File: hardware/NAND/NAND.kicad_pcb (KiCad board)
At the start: 2 copper layers, 53.3 x 86.4 mm, 10 parts, among them J1 Conn_02x33_Odd_Even, J2 Conn_02x33_Odd_Even, J3 DBG, J4 Left, J5 Right

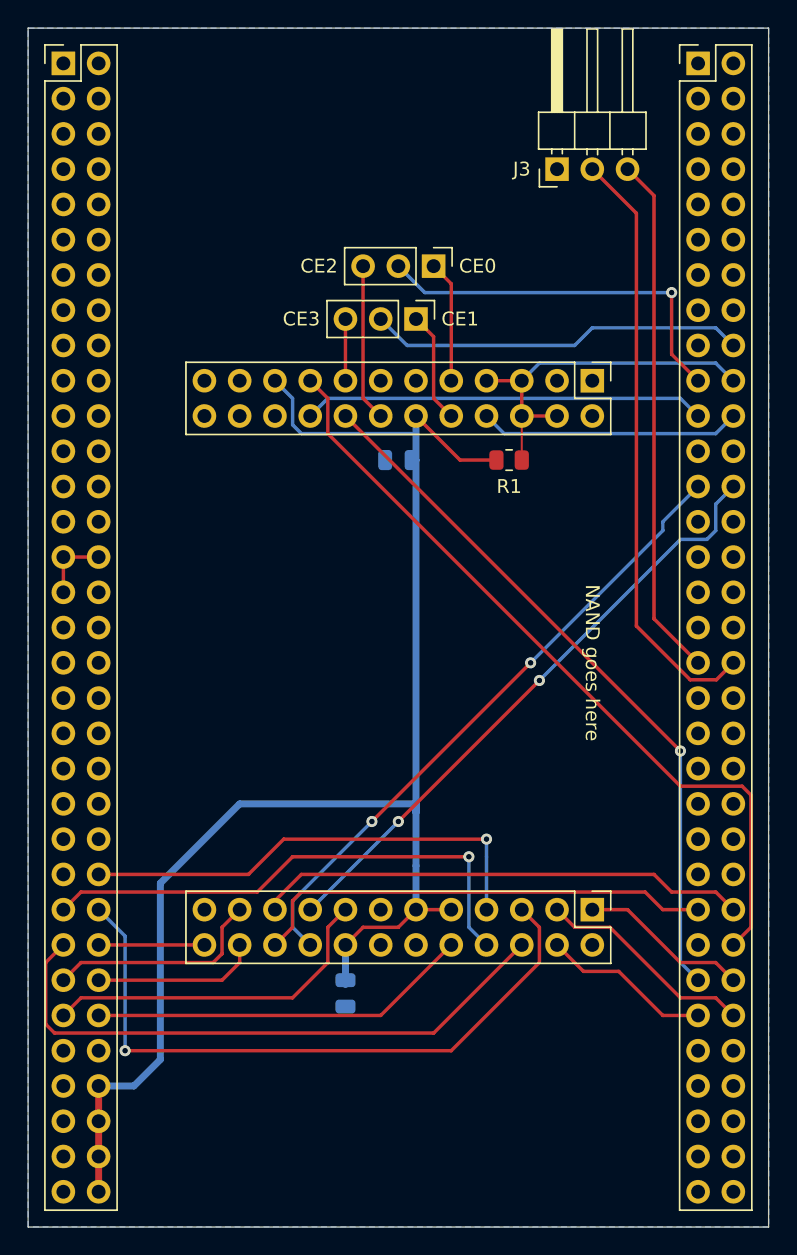
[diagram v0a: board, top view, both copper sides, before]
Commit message: hardware: NAND top to rev.B
+ Modified J3 DBG to break out SWO and GPIO pins

+ FSMC CE2 can be switched to any of NAND CEx

+ Added pull-ups for NAND CEx
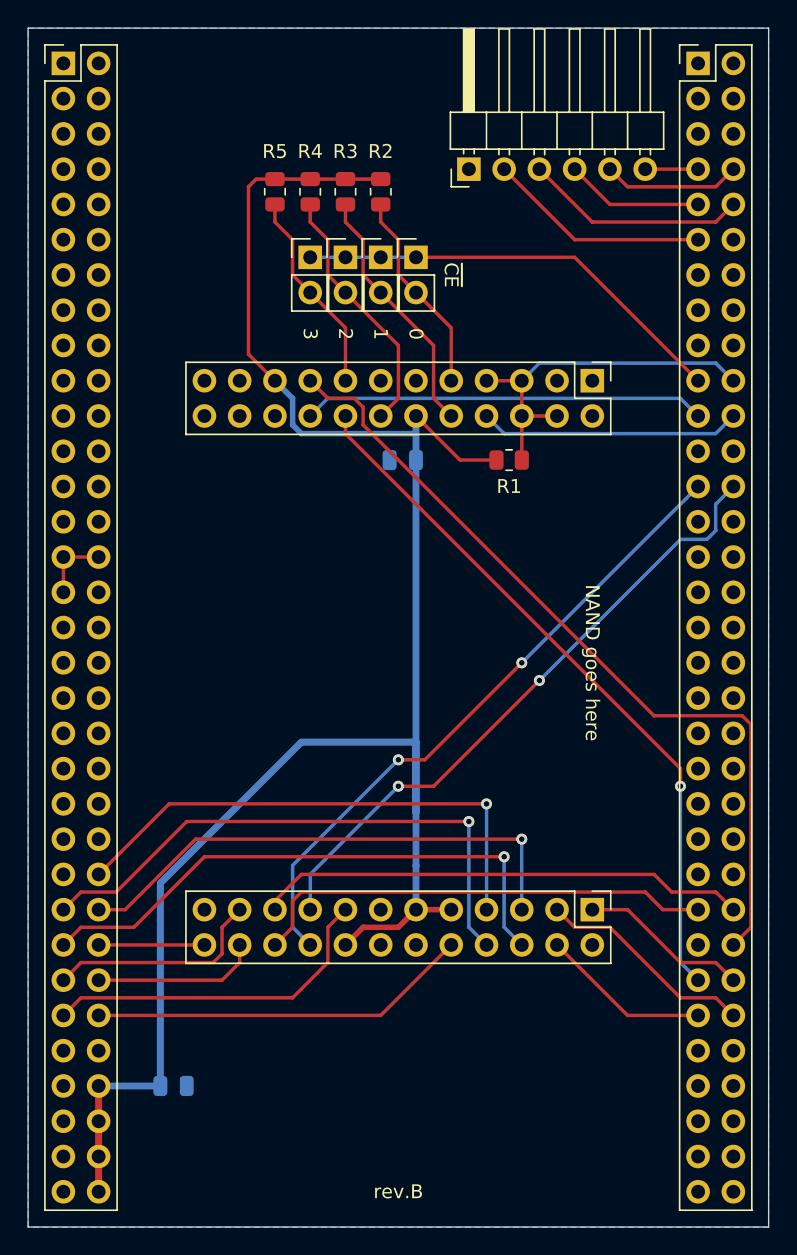
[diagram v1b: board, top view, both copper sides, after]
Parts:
- added JP3: CE2, Connector_PinHeader_2.54mm:PinHeader_1x02_P2.54mm_Vertical, F.Cu at (121.9, 90.2)
- added JP4: CE3, Connector_PinHeader_2.54mm:PinHeader_1x02_P2.54mm_Vertical, F.Cu at (119.4, 90.2)
- added R2: 10k, Resistor_SMD:R_0805_2012Metric, F.Cu at (124.5, 85.4)
- added R3: 10k, Resistor_SMD:R_0805_2012Metric, F.Cu at (121.9, 85.4)
- added R4: 10k, Resistor_SMD:R_0805_2012Metric, F.Cu at (119.4, 85.4)
- added R5: 10k, Resistor_SMD:R_0805_2012Metric, F.Cu at (116.8, 85.4)
- J1: value Conn_02x33_Odd_Even -> Left
- J2: value Conn_02x33_Odd_Even -> Right
- J3: footprint Connector_PinHeader_2.54mm:PinHeader_1x03_P2.54mm_Horizontal -> Connector_PinHeader_2.54mm:PinHeader_1x06_P2.54mm_Horizontal
- JP1: value CE0 SEL -> CE0; footprint Connector_PinHeader_2.54mm:PinHeader_1x03_P2.54mm_Vertical -> Connector_PinHeader_2.54mm:PinHeader_1x02_P2.54mm_Vertical
- JP2: value CE1 SEL -> CE1; footprint Connector_PinHeader_2.54mm:PinHeader_1x03_P2.54mm_Vertical -> Connector_PinHeader_2.54mm:PinHeader_1x02_P2.54mm_Vertical
- moved C2 14.1 mm to (109.5, 149.9), turned to 180 degrees
- moved J3 6.35 mm to (130.8, 83.8)
- moved JP2 5.12 mm to (124.5, 90.2), turned to 0 degrees
- moved JP1 1.42 mm to (127.0, 90.2), turned to 0 degrees
- moved C1 0.32 mm to (126.0, 104.8)
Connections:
- J1 pad 31: GND -> (no net)
- J2 pad 10: (no net) -> PB4
- J2 pad 11: (no net) -> PB3
- J2 pad 18: G9 -> (no net)
- J2 pad 19: D7 -> ~CE
- J2 pad 35: A10 -> (no net)
- J2 pad 36: A9 -> (no net)
- J2 pad 7: (no net) -> PB7
- J2 pad 8: (no net) -> PB6
- J2 pad 9: (no net) -> PB5
- J3 pad 2: A9 -> PB3
- J3 pad 3: A10 -> PB4
- JP1 pad 1: ~CE0 -> ~CE
- JP1 pad 2: D7 -> ~CE0
- JP2 pad 1: ~CE1 -> ~CE
- JP2 pad 2: G9 -> ~CE1
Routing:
- net A9: track 43.3 -> 0.00 mm
- net A10: track 37.7 -> 0.00 mm
- net ~CE: track 0.00 -> 31.6 mm
- net +3V3: track 114.3 -> 143.1 mm
- net D7: track 27.6 -> 0.00 mm, vias 1 -> 0
- net G9: track 27.2 -> 0.00 mm
- net PB4: track 0.00 -> 16.1 mm
- net PB3: track 0.00 -> 16.1 mm
- net ~CE1: track 8.04 -> 18.4 mm
- net ~CE3: track 4.45 -> 14.8 mm
- net IO6: track 47.8 -> 37.7 mm
- net PB6: track 0.00 -> 9.94 mm
- net PB5: track 0.00 -> 9.94 mm
- net ~CE2: track 11.3 -> 18.4 mm
- net ~CE0: track 8.78 -> 14.8 mm
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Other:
- net class Default: trace_width 0.15 -> 0.25
- board text added: "0"
- board text added: "1"
- board text added: "2"
- board text added: "3"
- board text added: "rev.B"
- board text added: "~CE"
- board text removed: "CE0"
- board text removed: "CE1"
- board text removed: "CE2"
- board text removed: "CE3"

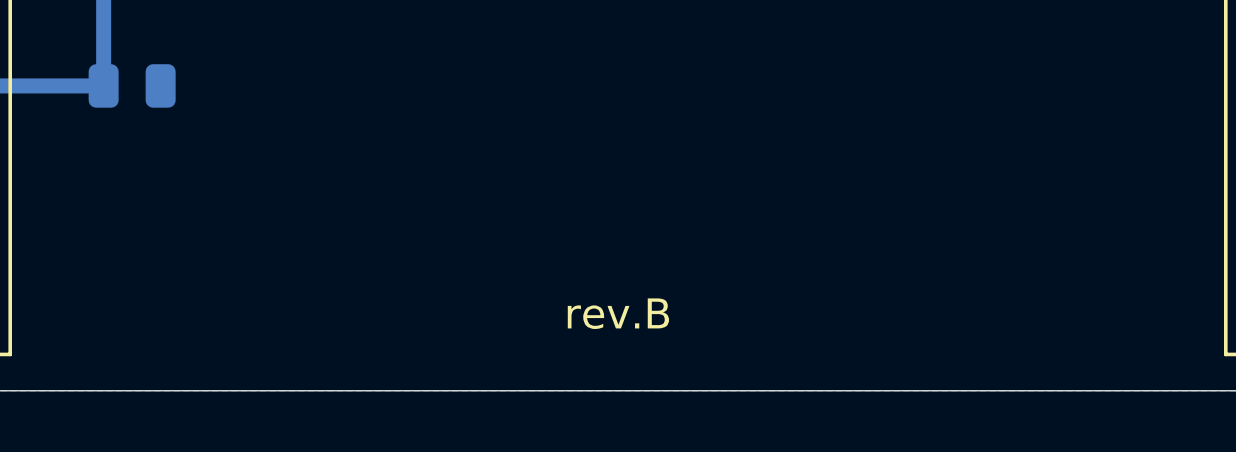
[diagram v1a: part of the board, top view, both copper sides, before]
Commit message: hardware: update top board labels
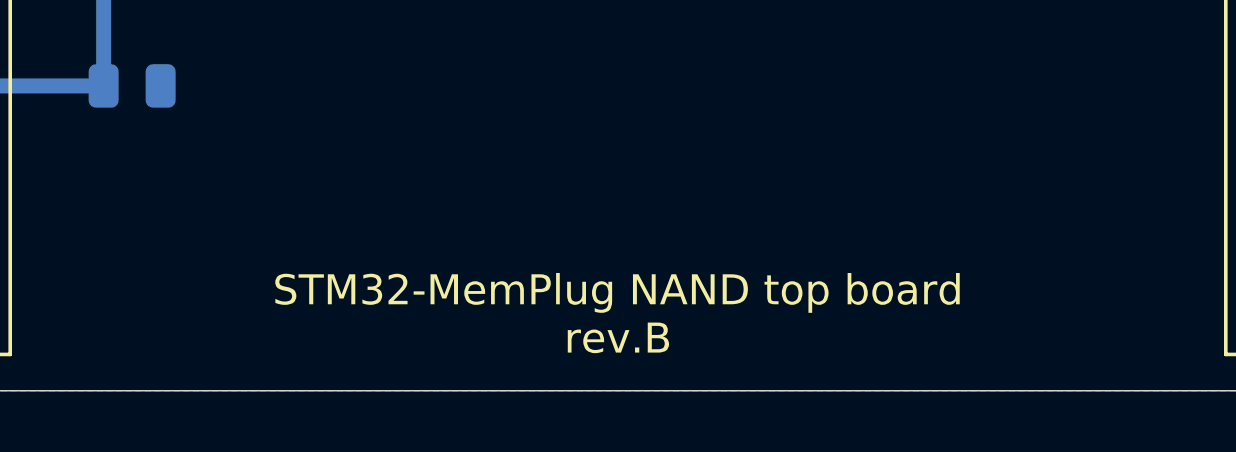
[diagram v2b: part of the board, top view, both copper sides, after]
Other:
- board text added: "STM32-MemPlug NAND top board rev.B"
- board text removed: "rev.B"

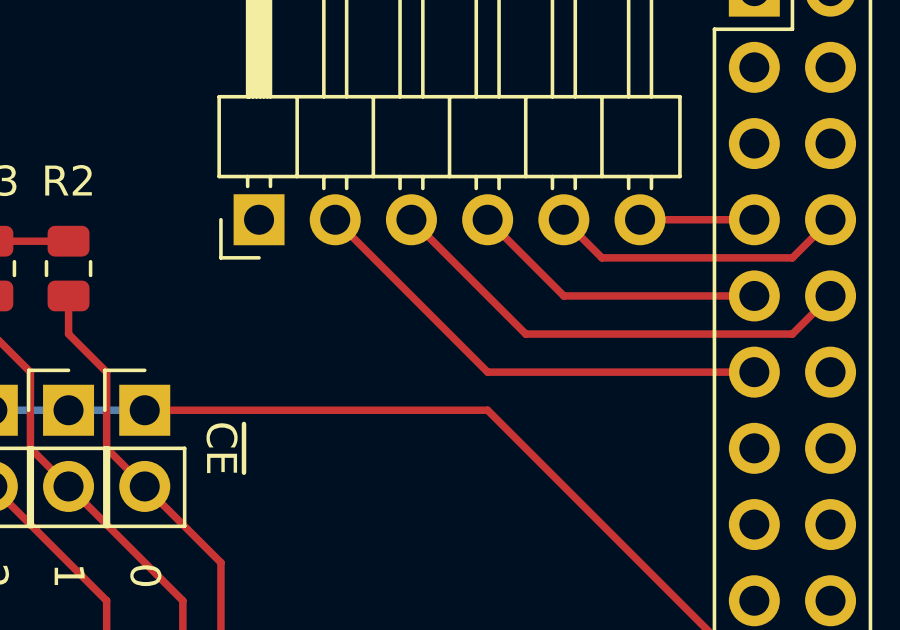
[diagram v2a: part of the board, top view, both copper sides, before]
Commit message: refreshed carrier boards and added missing symbol libs
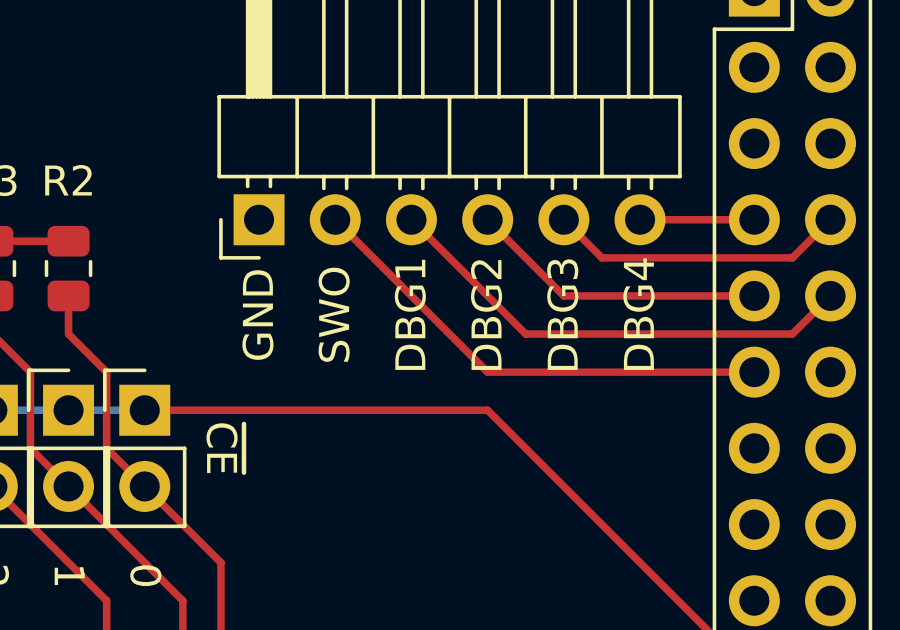
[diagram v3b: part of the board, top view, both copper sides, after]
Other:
- board text added: "DBG1"
- board text added: "DBG2"
- board text added: "DBG3"
- board text added: "DBG4"
- board text added: "GND"
- board text added: "SWO"
